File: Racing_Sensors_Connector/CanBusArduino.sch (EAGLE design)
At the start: 15 parts, among them Y1 16MHz

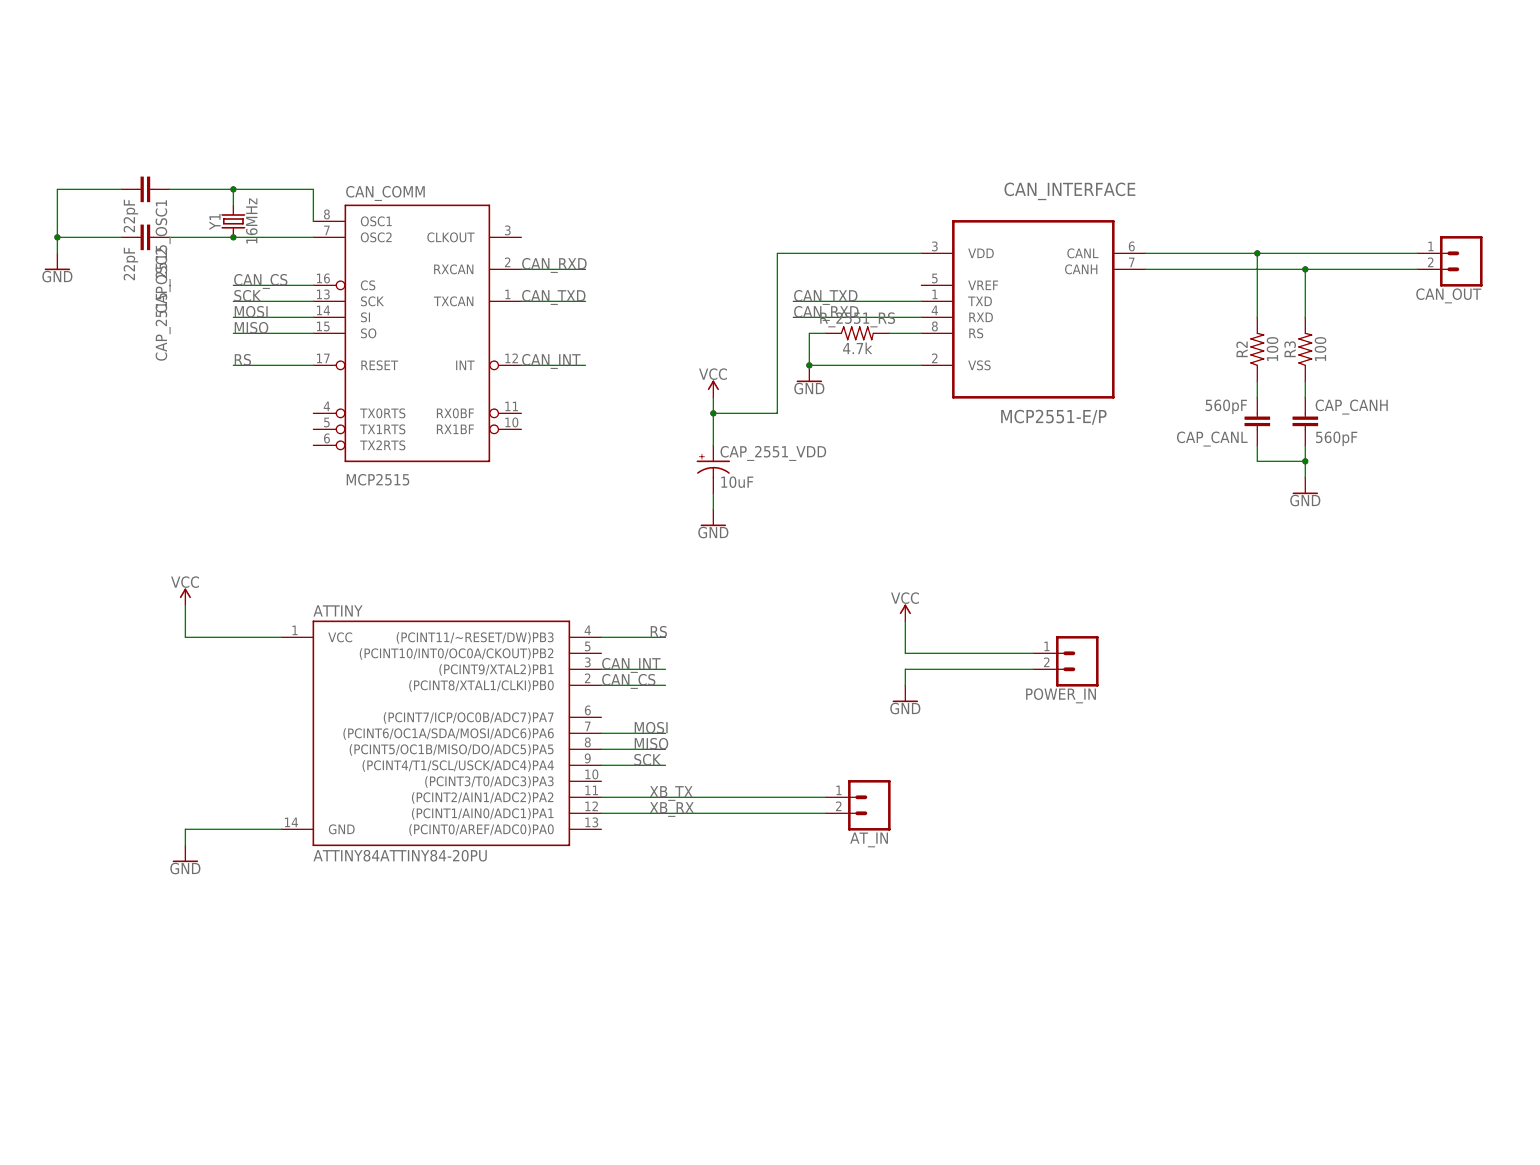
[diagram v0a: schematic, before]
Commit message: Add CAN communiator for ATmega328P
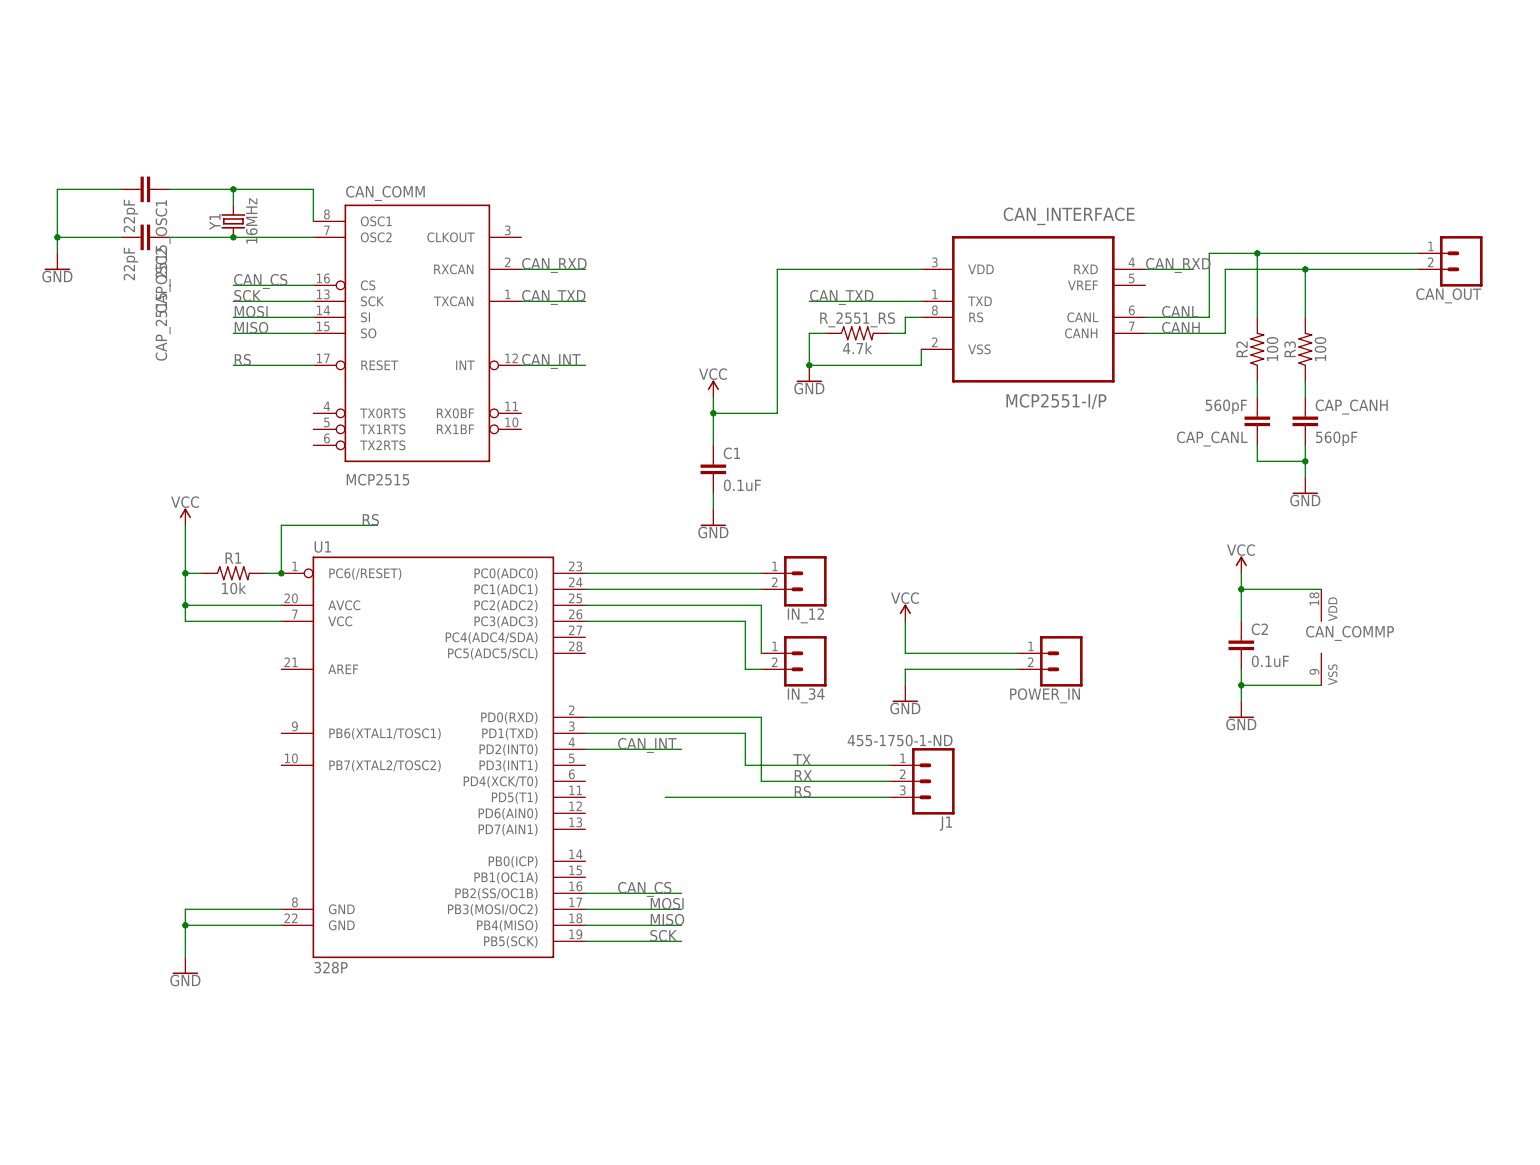
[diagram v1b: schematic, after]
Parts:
- removed ATTINY: ATTINY84ATTINY84-20PU, SparkFun-IC-Microcontroller:ATTINY84ATTINY84-20PU
- removed AT_IN: (no value), SparkFun-Connectors:CONN_023.5MM
- removed CAP_2551_VDD: 10uF, SparkFun-Capacitors:10UF-POLAR-RADIAL-2.5MM-25V-20%
- added C1, C2: 0.1uF, SparkFun-Capacitors:0.1UF-0402-16V-10%
- added IN_12, IN_34: (no value), SparkFun-Connectors:CONN_023.5MM
- added J1: 455-1750-1-ND, SparkFun-Connectors:CONN_03
- added R1: 10k, SparkFun-Resistors:10KOHM-0603-1/10W-1%
- added U1: 328P, SparkFun-IC-Microcontroller:ATMEGA328P_PDIP
- CAN_INTERFACE: value MCP2551-E/P -> MCP2551-I/P; device mcp2551dip:MCP2551-E/P -> can_transceiver:MCP2551-I/P
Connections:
- net N$2 renamed CI_RS
- net N$3 renamed CANL
- net N$4 renamed CANH
- removed net XB_RX: ATTINY.(PCINT1/AIN0/ADC1)PA1, AT_IN.2
- removed net XB_TX: ATTINY.(PCINT2/AIN1/ADC2)PA2, AT_IN.1
- new net IN1: IN_12.1, U1.PC0(ADC0)
- new net IN2: IN_12.2, U1.PC1(ADC1)
- new net IN3: IN_34.1, U1.PC2(ADC2)
- new net IN4: IN_34.2, U1.PC3(ADC3)
- new net RX: J1.2, U1.PD0(RXD)
- new net TX: J1.1, U1.PD1(TXD)
- net CAN_CS: now also U1.PB2(SS/OC1B); no longer ATTINY.(PCINT8/XTAL1/CLKI)PB0
- net CAN_INT: now also U1.PD2(INT0); no longer ATTINY.(PCINT9/XTAL2)PB1
- net CAN_RXD: now also CAN_INTERFACE.RXD
- net CAN_TXD: now also CAN_INTERFACE.TXD
- net GND: now also C1.2, C2.2, CAN_COMMP.VSS, CAN_INTERFACE.VSS, U1.GND@1, U1.GND@2; no longer ATTINY.GND, CAP_2551_VDD.-
- net MISO: now also U1.PB4(MISO); no longer ATTINY.(PCINT5/OC1B/MISO/DO/ADC5)PA5
- net MOSI: now also U1.PB3(MOSI/OC2); no longer ATTINY.(PCINT6/OC1A/SDA/MOSI/ADC6)PA6
- net RS: now also J1.3, R1.2, U1.PC6(/RESET); no longer ATTINY.(PCINT11/~RESET/DW)PB3
- net SCK: now also U1.PB5(SCK); no longer ATTINY.(PCINT4/T1/SCL/USCK/ADC4)PA4
- net VCC: now also C1.1, C2.1, CAN_COMMP.VDD, R1.1, U1.AVCC, U1.VCC; no longer ATTINY.VCC, CAP_2551_VDD.+
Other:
- moved on the sheet: POWER_IN

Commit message: Update drawing
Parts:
- removed CAN_OUT, IN_12, IN_34, POWER_IN: (no value), SparkFun-Connectors:CONN_023.5MM
- added ADC0/1, ADC2/3, ADC4/5, CANH/L, DIO, PWR: (no value), SparkFun-Connectors:CONN_02POLAR
- renumbered J1 to PRGM
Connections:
- net N$1 renamed OSC1
- net N$5 renamed OSC2
- removed net IN1: IN_12.1, U1.PC0(ADC0)
- removed net IN2: IN_12.2, U1.PC1(ADC1)
- removed net IN3: IN_34.1, U1.PC2(ADC2)
- removed net IN4: IN_34.2, U1.PC3(ADC3)
- new net A0: ADC0/1.1, U1.PC0(ADC0)
- new net A1: ADC0/1.2, U1.PC1(ADC1)
- new net A2: ADC2/3.1, U1.PC2(ADC2)
- new net A3: ADC2/3.2, U1.PC3(ADC3)
- new net A4: ADC4/5.1, U1.PC4(ADC4/SDA)
- new net A5: ADC4/5.2, U1.PC5(ADC5/SCL)
- new net D3: DIO.2, U1.PD3(INT1)
- new net D4: DIO.1, U1.PD4(XCK/T0)
- net CANH: now also CANH/L.2; no longer CAN_OUT.2
- net CANL: now also CANH/L.1; no longer CAN_OUT.1
- net GND: now also PWR.2; no longer POWER_IN.2
- net VCC: now also PWR.1; no longer POWER_IN.1
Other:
- moved on the sheet: C1

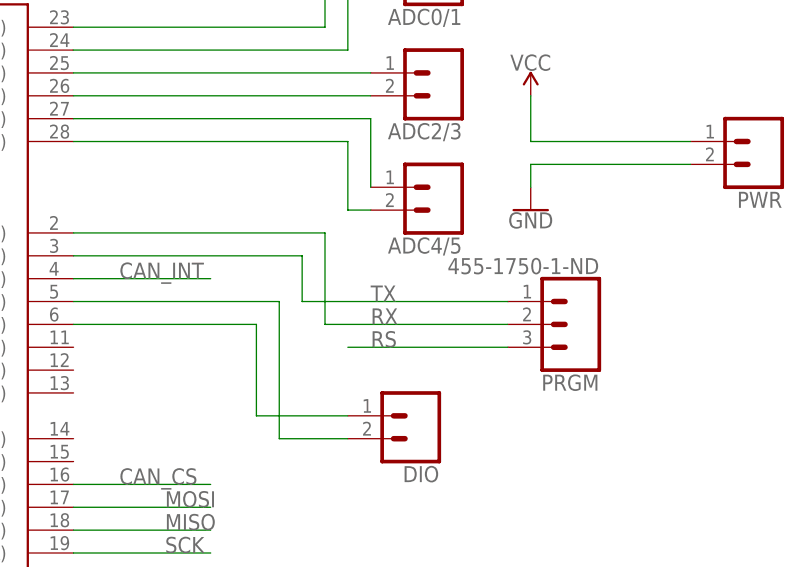
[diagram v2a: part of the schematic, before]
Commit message: Move programming header to the side
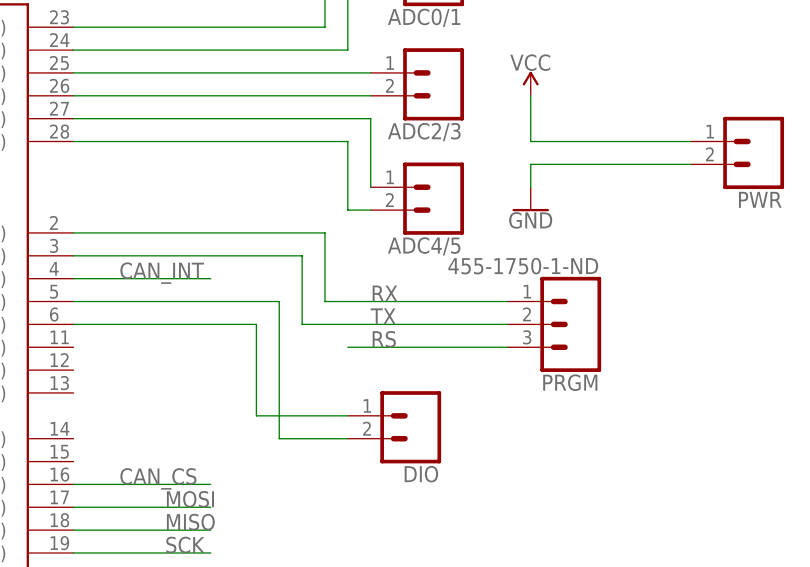
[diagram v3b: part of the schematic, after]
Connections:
- net RX: now also PRGM.1; no longer PRGM.2
- net TX: now also PRGM.2; no longer PRGM.1
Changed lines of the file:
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@@
 <pinref part="U1" gate="G$1" pin="PD0(RXD)"/>
 <wire x1="91.44" y1="68.58" x2="119.38" y2="68.58" width="0.1524" layer="91"/>
-<wire x1="119.38" y1="58.42" x2="119.38" y2="68.58" width="0.1524" layer="91"/>
-<pinref part="PRGM" gate="J$1" pin="2"/>
-<wire x1="139.7" y1="58.42" x2="119.38" y2="58.42" width="0.1524" layer="91"/>
-<label x="124.46" y="58.42" size="1.778" layer="95"/>
+<pinref part="PRGM" gate="J$1" pin="1"/>
+<wire x1="139.7" y1="60.96" x2="119.38" y2="60.96" width="0.1524" layer="91"/>
+<label x="124.46" y="60.96" size="1.778" layer="95"/>
+<wire x1="119.38" y1="68.58" x2="119.38" y2="60.96" width="0.1524" layer="91"/>
 </segment>
 </net>
@@
 <pinref part="U1" gate="G$1" pin="PD1(TXD)"/>
 <wire x1="91.44" y1="66.04" x2="116.84" y2="66.04" width="0.1524" layer="91"/>
-<wire x1="116.84" y1="66.04" x2="116.84" y2="60.96" width="0.1524" layer="91"/>
-<pinref part="PRGM" gate="J$1" pin="1"/>
-<wire x1="139.7" y1="60.96" x2="116.84" y2="60.96" width="0.1524" layer="91"/>
-<label x="124.46" y="60.96" size="1.778" layer="95"/>
+<wire x1="116.84" y1="66.04" x2="116.84" y2="58.42" width="0.1524" layer="91"/>
+<pinref part="PRGM" gate="J$1" pin="2"/>
+<wire x1="139.7" y1="58.42" x2="116.84" y2="58.42" width="0.1524" layer="91"/>
+<label x="124.46" y="58.42" size="1.778" layer="95"/>
 </segment>
 </net>

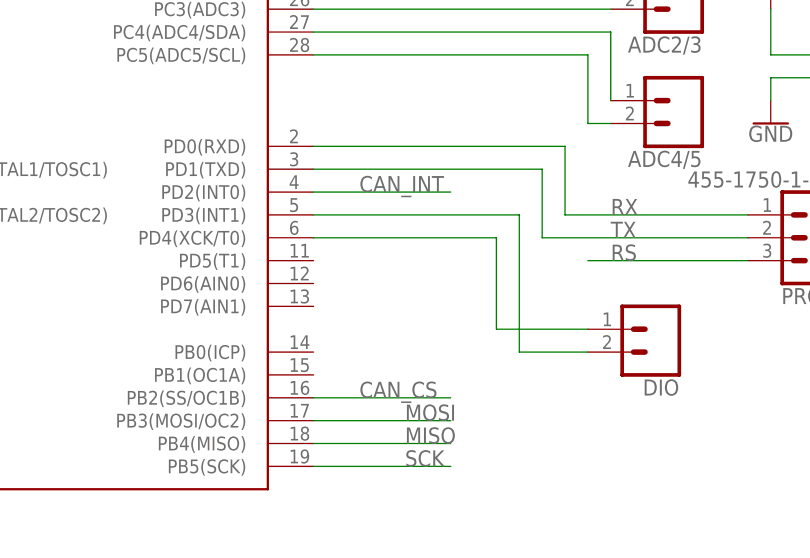
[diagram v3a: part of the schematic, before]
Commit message: Move digital pin 6 to 11 (4 to 5)
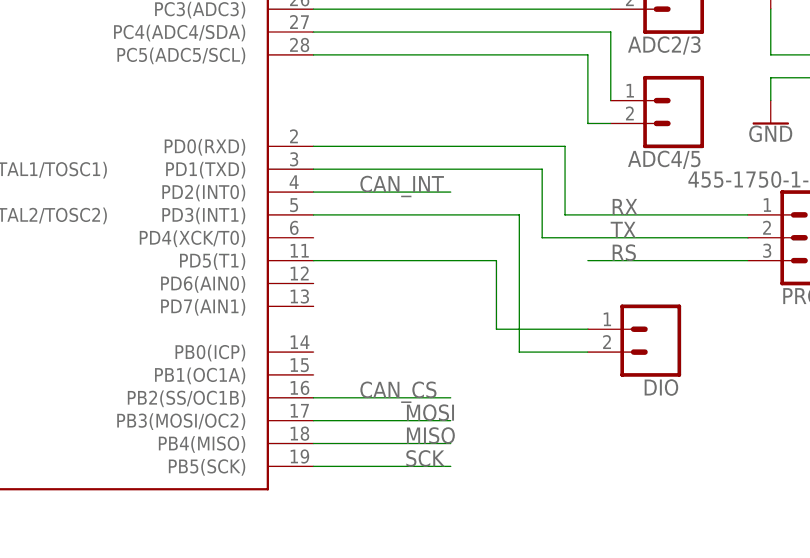
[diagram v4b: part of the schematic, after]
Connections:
- net D4: now also U1.PD5(T1); no longer U1.PD4(XCK/T0)
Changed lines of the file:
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@@
 <net name="D4" class="0">
 <segment>
-<pinref part="U1" gate="G$1" pin="PD4(XCK/T0)"/>
-<wire x1="91.44" y1="58.42" x2="111.76" y2="58.42" width="0.1524" layer="91"/>
-<wire x1="111.76" y1="58.42" x2="111.76" y2="48.26" width="0.1524" layer="91"/>
 <wire x1="111.76" y1="48.26" x2="121.92" y2="48.26" width="0.1524" layer="91"/>
 <pinref part="DIO" gate="G$1" pin="1"/>
+<wire x1="111.76" y1="48.26" x2="111.76" y2="55.88" width="0.1524" layer="91"/>
+<pinref part="U1" gate="G$1" pin="PD5(T1)"/>
+<wire x1="111.76" y1="55.88" x2="91.44" y2="55.88" width="0.1524" layer="91"/>
 </segment>
 </net>

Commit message: Redesign PCB slightly
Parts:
- C1, C2: device SparkFun-Capacitors:0.1UF-0402-16V-10% -> SparkFun-Capacitors:0.1UF-0603-100V-10%
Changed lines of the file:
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@@
 <part name="U1" library="SparkFun-IC-Microcontroller" deviceset="ATMEGA328P_PDIP" device="" value="328P"/>
 <part name="R1" library="SparkFun-Resistors" deviceset="10KOHM" device="-0603-1/10W-1%" value="10k"/>
-<part name="C1" library="SparkFun-Capacitors" deviceset="0.1UF" device="-0402-16V-10%" value="0.1uF"/>
-<part name="C2" library="SparkFun-Capacitors" deviceset="0.1UF" device="-0402-16V-10%" value="0.1uF"/>
+<part name="C1" library="SparkFun-Capacitors" deviceset="0.1UF" device="-0603-100V-10%" value="0.1uF"/>
+<part name="C2" library="SparkFun-Capacitors" deviceset="0.1UF" device="-0603-100V-10%" value="0.1uF"/>
 <part name="SUPPLY4" library="SparkFun-PowerSymbols" deviceset="VCC" device=""/>
 <part name="GND7" library="SparkFun-PowerSymbols" deviceset="GND" device=""/>

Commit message: Start redesign
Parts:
- removed C2: 0.1uF, SparkFun-Capacitors:0.1UF-0603-100V-10%
- removed CAN_COMM: MCP2515, SparkFun-IC-Comms:MCP2515(MCP2510)P
- removed CAP_2515_OSC1, CAP_2515_OSC2: 22pF, SparkFun-Capacitors:22PF-0603-50V-5%
- removed DIO: (no value), SparkFun-Connectors:CONN_02POLAR
- removed R1: 10k, SparkFun-Resistors:10KOHM-0603-1/10W-1%
- removed U1: 328P, SparkFun-IC-Microcontroller:ATMEGA328P_PDIP
- removed Y1: 16MHz, SparkFun-Clocks:CRYSTALPTH-HC49US
- added ADC6/7, CANH/L2, I2C, TX/RX: (no value), SparkFun-Connectors:CONN_02POLAR
- added BYP2: 0.1uF, SparkFun-Capacitors:0.1UF-0603-25V-(+80/-20%)
- added COSC1, COSC2: 22pF, SparkFun-Capacitors:22PF-0603-50V-5%
- added ISP: (no value), SparkFun-Connectors:CONN_03X22X3_SILK_MALE_PTH
- added OSC: 16MHz, SparkFun-Clocks:CRYSTALPTH-HC49US
- added RST_PULLUP, SD_PULLUP: 10k, SparkFun-Resistors:10KOHM-0603-1/10W-1%
- added U2: SPARKFUN_USD-SOCKETSMD, microSD-Breakout-v14:SPARKFUN_USD-SOCKETSMD
- added U3: AT90CAN128-16AI, _hhn_at90can32_64_128_v2:AT90CAN128-16AI
- PRGM: value 455-1750-1-ND -> (none)
- renumbered C1 to BYP1, CANH/L to CANH/L1
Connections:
- removed net CAN_CS: CAN_COMM>NAME.CS, U1.PB2(SS/OC1B)
- removed net CAN_INT: CAN_COMM>NAME.INT, U1.PD2(INT0)
- removed net D3: DIO.2, U1.PD3(INT1)
- removed net D4: DIO.1, U1.PD5(T1)
- removed net RS: CAN_COMM>NAME.RESET, PRGM.3, R1.2, U1.PC6(/RESET)
- new net A6: ADC6/7.1, U3.PF6(ADC6/TDO)
- new net A7: ADC6/7.2, U3.PF7(ADC7/TDI)
- new net RESET: ISP.5, PRGM.3, RST_PULLUP.1, U3.!RESET
- new net RX1: TX/RX.2, U3.(RXD1/INT2)PD2
- new net SCL: I2C.2, U3.(SCL/INT0)PD0
- new net SDA: I2C.1, U3.(SDA/INT1)PD1
- new net SD_CD: SD_PULLUP.1, U2.CD2, U3.(AD7)PA7
- new net SD_CS: U2.CS, U3.(AD6)PA6
- new net TX1: TX/RX.1, U3.(TXD1/INT3)PD3
- net A0: now also U3.PF0(ADC0); no longer U1.PC0(ADC0)
- net A1: now also U3.PF1(ADC1); no longer U1.PC1(ADC1)
- net A2: now also U3.PF2(ADC2); no longer U1.PC2(ADC2)
- net A3: now also U3.PF3(ADC3); no longer U1.PC3(ADC3)
- net A4: now also U3.PF4(ADC4/TCK); no longer U1.PC4(ADC4/SDA)
- net A5: now also U3.PF5(ADC5/TMS); no longer U1.PC5(ADC5/SCL)
- net CANH: now also CANH/L2.2
- net CANL: now also CANH/L2.1
- net CAN_RXD: now also U3.(RXCAN/T1)PD6; no longer CAN_COMM>NAME.RXCAN
- net CAN_TXD: now also U3.(TXCAN/XCK1)PD5; no longer CAN_COMM>NAME.TXCAN
- net GND: now also BYP2.2, COSC1.2, COSC2.2, ISP.6, U2.GND, U2.SHIELD1, U2.SHIELD2, U3.GND@1, U3.GND@2, U3.GND@3; no longer C2.2, CAN_COMMP.VSS, CAP_2515_OSC1.2, CAP_2515_OSC2.2, U1.GND@1, U1.GND@2
- net MISO: now also ISP.1, U2.DO, U3.(MISO)PB3; no longer CAN_COMM>NAME.SO, U1.PB4(MISO)
- net MOSI: now also ISP.4, U2.DI, U3.(MOSI)PB2; no longer CAN_COMM>NAME.SI, U1.PB3(MOSI/OC2)
- net OSC1: now also COSC1.1, OSC.2, U3.XTAL1; no longer CAN_COMM>NAME.OSC1, CAP_2515_OSC1.1, Y1.2
- net OSC2: now also COSC2.1, OSC.1, U3.XTAL2; no longer CAN_COMM>NAME.OSC2, CAP_2515_OSC2.1, Y1.1
- net RX: now also U3.(RXD0/PDI)PE0; no longer U1.PD0(RXD)
- net SCK: now also ISP.3, U2.SCK, U3.(SCK)PB1; no longer CAN_COMM>NAME.SCK, U1.PB5(SCK)
- net TX: now also U3.(TXD0/PDO)PE1; no longer U1.PD1(TXD)
- net VCC: now also BYP2.1, ISP.2, RST_PULLUP.2, SD_PULLUP.2, U2.VCC, U3.AVCC, U3.VCC@1, U3.VCC@2; no longer C2.1, CAN_COMMP.VDD, R1.1, U1.AVCC, U1.VCC
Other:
- note added: "3"
- note added: "Backup Arduino programmer"
- note added: "Programming ISP header for Atmel ICE"
- note added: "RS Pin: resistor value controls slope"
- note added: "SD_CD HIGH when card inserted LOW when card removed"
- moved on the sheet: ADC0/1, ADC2/3, ADC4/5, PRGM, PWR

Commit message: Before SD fix
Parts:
- removed CAN_INTERFACE: MCP2551-I/P, can_transceiver:MCP2551-I/P
- removed R_2551_RS: 4.7k, SparkFun-Resistors:4.7KOHM-0603-1/10W-1%
- added IFACE: MCP2561-E/SN, Volks73-MicrochipTechnology:MCP2561-E/SN
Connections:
- removed net CI_RS: CAN_INTERFACE.RS, R_2551_RS.2
- new net CAN_STBY: IFACEU$1.STBY, U3.(AD5)PA5
- net A0: now also ADC0/1.2; no longer ADC0/1.1
- net A1: now also ADC0/1.1; no longer ADC0/1.2
- net A2: now also ADC2/3.2; no longer ADC2/3.1
- net A3: now also ADC2/3.1; no longer ADC2/3.2
- net A4: now also ADC4/5.2; no longer ADC4/5.1
- net A5: now also ADC4/5.1; no longer ADC4/5.2
- net A6: now also ADC6/7.2; no longer ADC6/7.1
- net A7: now also ADC6/7.1; no longer ADC6/7.2
- net CANH: now also IFACEU$1.CANH; no longer CAN_INTERFACE.CANH
- net CANL: now also IFACEU$1.CANL; no longer CAN_INTERFACE.CANL
- net CAN_RXD: now also IFACEU$1.RXD; no longer CAN_INTERFACE.RXD
- net CAN_TXD: now also IFACEU$1.TXD; no longer CAN_INTERFACE.TXD
- net GND: now also IFACE-SUPPLY.VSS; no longer CAN_INTERFACE.VSS, R_2551_RS.1
- net VCC: now also IFACE-SUPPLY.VDD; no longer CAN_INTERFACE.VDD
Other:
- moved on the sheet: BYP1
